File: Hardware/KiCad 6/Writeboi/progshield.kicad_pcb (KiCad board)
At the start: 2 copper layers, 121.9 x 81.3 mm, 14 parts, among them J1 GB-CART, J2 AUX_POW, SW1 SW_Push, U1 SST39SF040

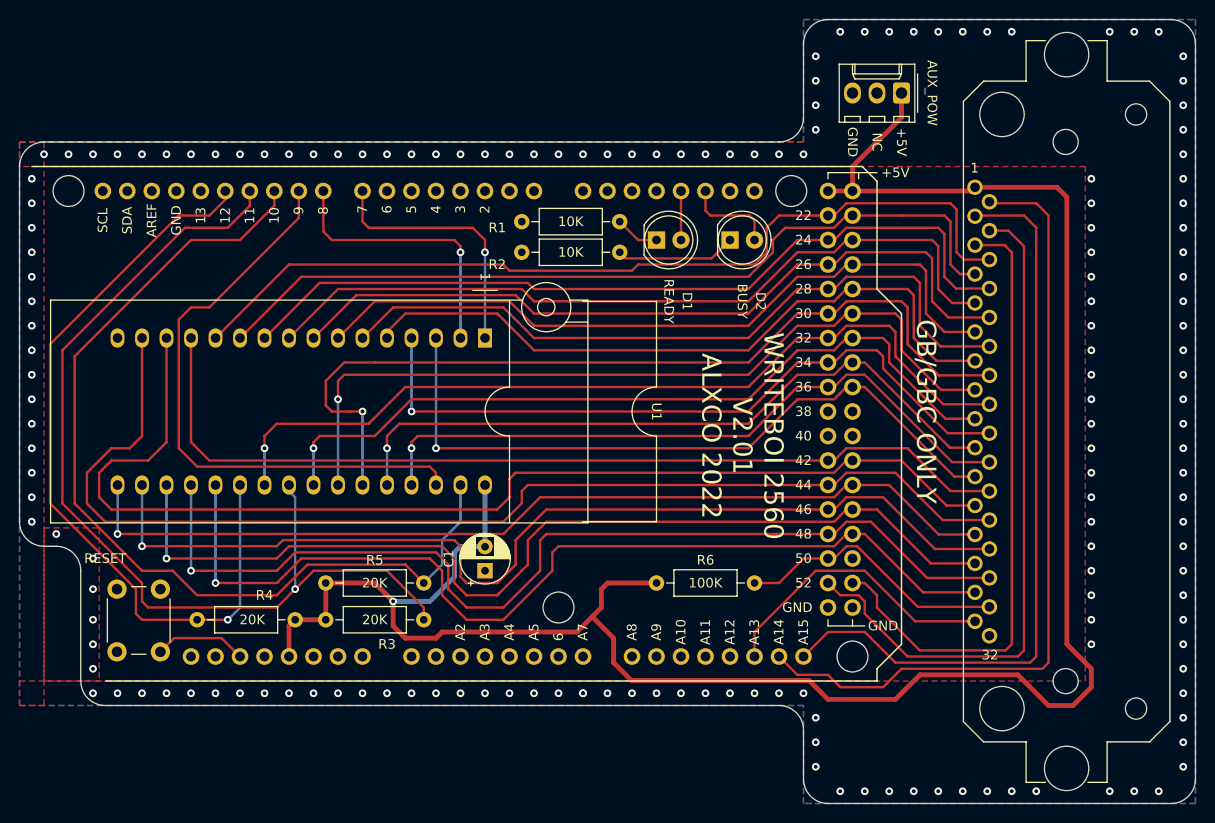
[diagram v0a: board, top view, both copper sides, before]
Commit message: Clean up Writeboi traces
Clean up disconnected traces
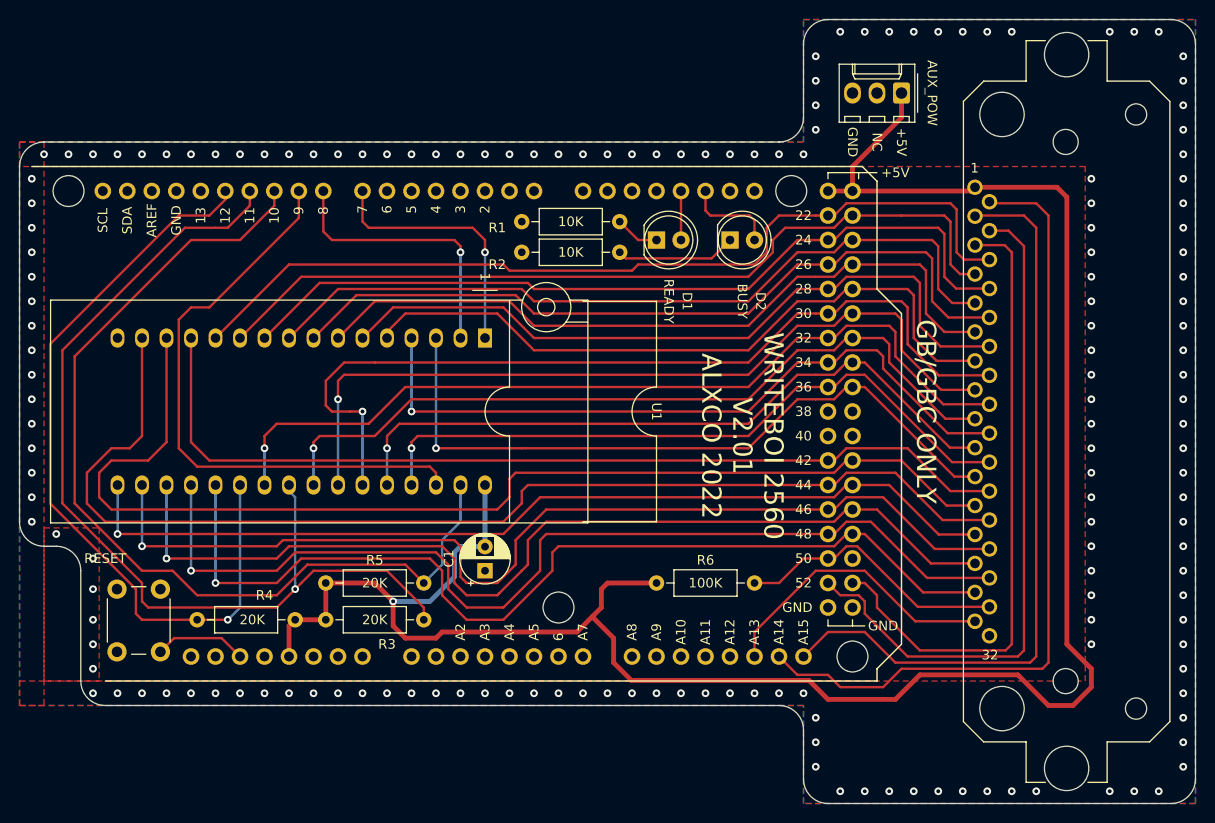
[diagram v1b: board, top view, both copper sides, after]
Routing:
- net /A12: track 75.1 -> 74.5 mm
- net /A6: track 76.5 -> 75.9 mm
- net Net-(XA1-PadD41): track 0.64 -> 0.00 mm
- net Net-(XA1-PadD40): track 0.64 -> 0.00 mm
- net Net-(XA1-PadD39): track 0.64 -> 0.00 mm
- net Net-(XA1-PadD38): track 0.64 -> 0.00 mm
- net Net-(D1-Pad1): track 5.23 -> 4.60 mm
- net GND: vias 164 -> 163
